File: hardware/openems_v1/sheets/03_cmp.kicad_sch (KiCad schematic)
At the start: 0 parts

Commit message: feat(hw): fecha esquemático v2 — sheets 01/02/03/05/07/11 desenhadas, ERC 0
- 01_power: nova — P-FET reverse (Q1) + F1 30A + SMBJ24CA + bulk 100µF/100nF,
  star GND (PGND/SGND/AGND) via PWR_FLAG na sheet produtora, VBAT limpo para
  o resto da placa (buck/LDO ficam no TPS65381A, sheet PMIC)
- 02_ckp / 03_cmp: CKP Hall (espelho do CMP) → MCU.PA0/PA1
- 05_analog: refeita do zero a partir do pinout_v2 (13 canais ADC), mapa
  pré-v2 descartado
- 11_mcu_h562: netlist U1 corrigido (lib_id não resolvia pinos — 100 pinos
  caíam na mesma net); globals PA0/PA1/PB4 sincronizados com as sheets acima
- 07_flex: pino corrigido para PB4 (pinout_v2)
- READMEs (hardware/openems_v1, docs/hw/schematic) actualizados ao estado
  real por sheet

Passos 1-5 do roadmap do esquemático fechados; ERC isolado por sheet em 0
erros (avisos residuais são globals sem sheet destino ainda — esperado).

Co-Authored-By: Claude Sonnet 5 <noreply@anthropic.com>
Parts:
- added C1: 330pF, Capacitor_SMD:C_0603_1608Metric, symbol Device:C
- added D1: 3V3 unidirectional, Diode_SMD:D_SOD-123, symbol Device:D_TVS
- added R1, R2: 10k, Resistor_SMD:R_0603_1608Metric, symbol Device:R
- added R3: 15k, Resistor_SMD:R_0603_1608Metric, symbol Device:R
- added R4: 330, Resistor_SMD:R_0603_1608Metric, symbol Device:R
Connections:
- new net +5V_SENS_A: R1.1
- new net AGND: C1.2, D1.2 (A2)
- new net J1.CMP_SIG: D1.1 (A1), R1.2, R2.1
- new net MCU.PA1: C1.1, R4.2
- new net N_CMP_DIV: R2.2, R3.1, R4.1
- new net SGND: R3.2
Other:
- note added: "Sheet 03 — CMP Hall → MCU.PA1 | mirror twin of 02_ckp"

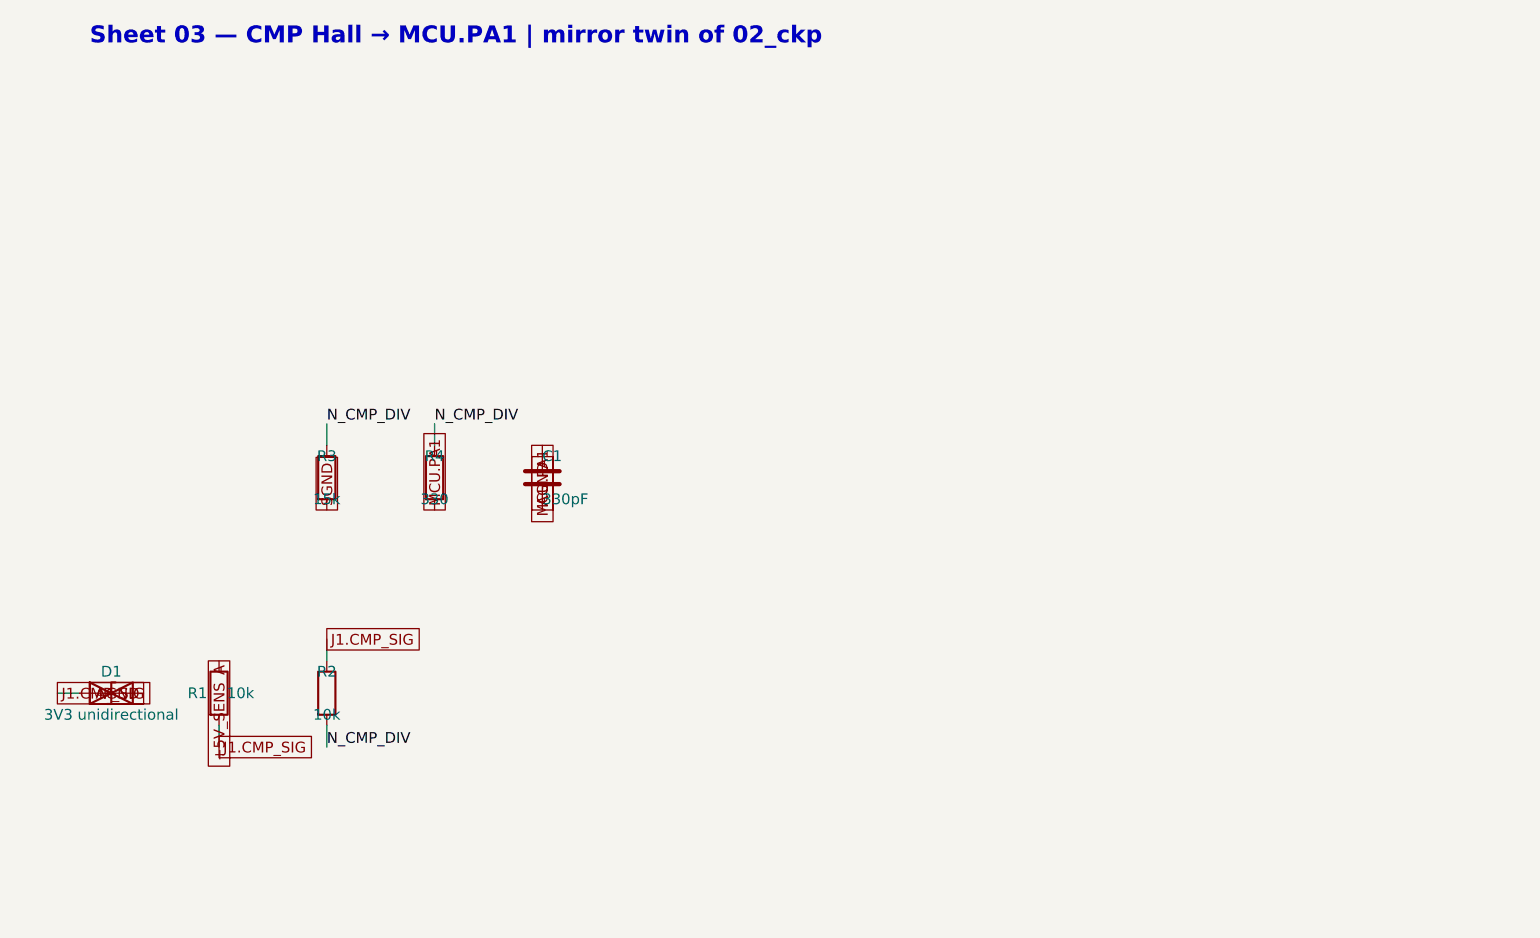
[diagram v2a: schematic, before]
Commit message: fix(hw): corrige legibilidade de 03_cmp e 07_flex — mesmo tratamento
03_cmp era clone directo do 02_ckp pré-correção (mesmo pitch de 12.7mm,
mesma sobreposição). 07_flex tinha o mesmo padrão em menor escala.
Reconstruídas com o layout validado no commit anterior — conectividade
idêntica, ERC 0 erros nas duas.

Co-Authored-By: Claude Sonnet 5 <noreply@anthropic.com>
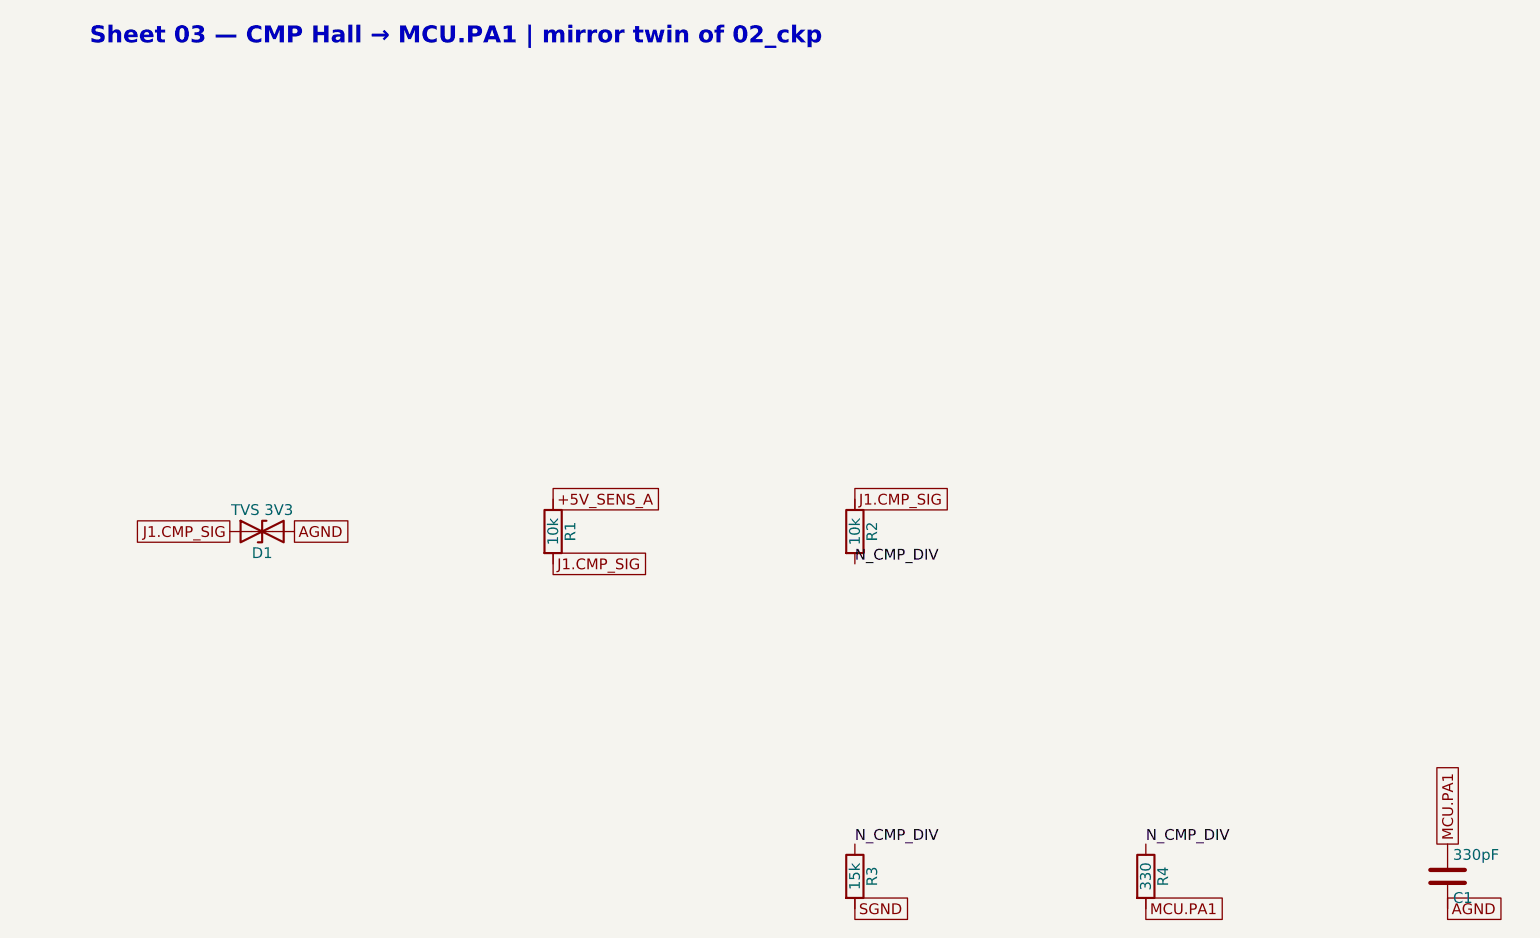
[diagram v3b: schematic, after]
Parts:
- D1: value 3V3 unidirectional -> TVS 3V3
